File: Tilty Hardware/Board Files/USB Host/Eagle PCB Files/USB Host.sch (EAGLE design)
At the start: 14 parts, among them Q1 12MHz, U1 MAX3421E

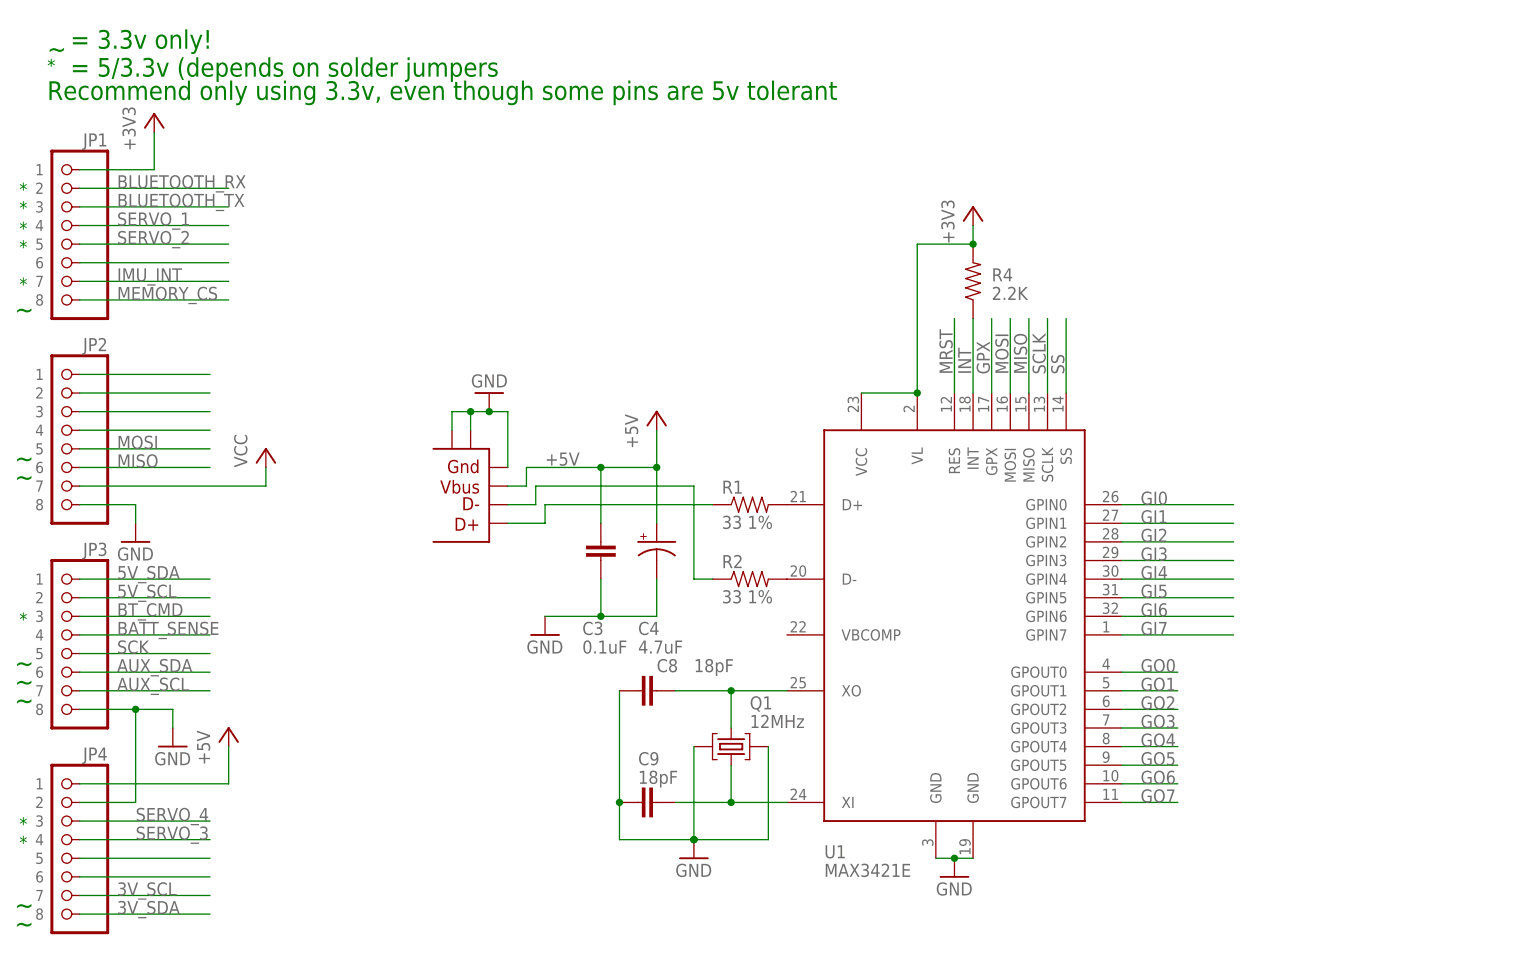
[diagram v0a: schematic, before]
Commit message: Added some datasheets, USB Host work
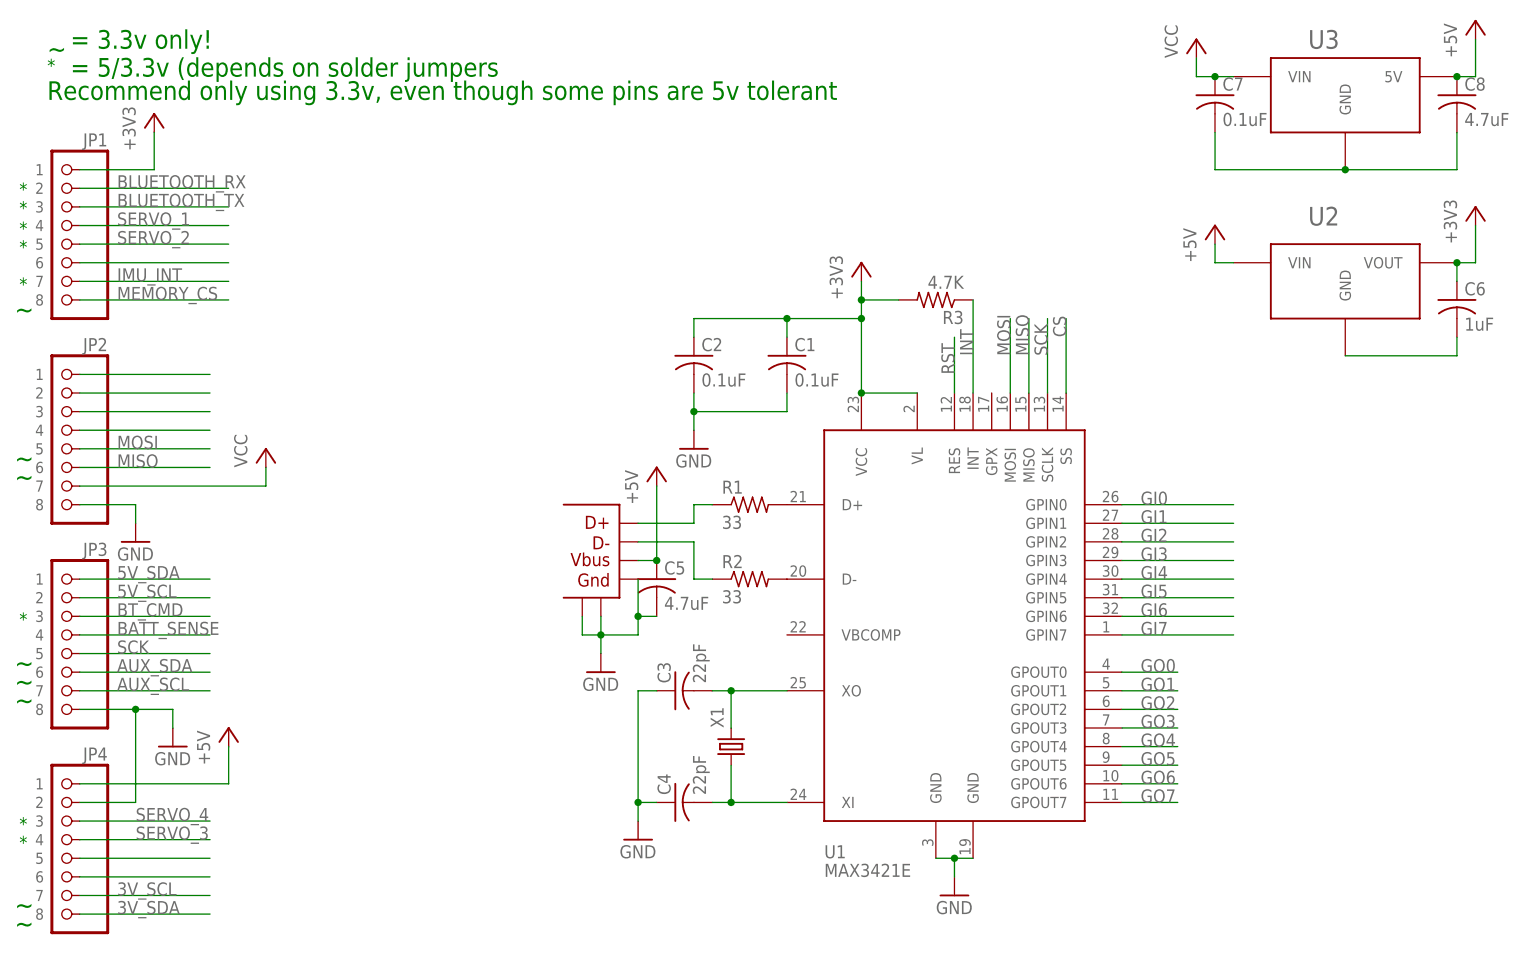
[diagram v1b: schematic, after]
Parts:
- removed C9: 18pF, CH_passive:CAP0603
- removed Q1: 12MHz, CH_passive:CRYSTAL_SH
- removed R4: 2.2K, CH_passive:RESISTOR0603
- added C1, C2, C7: 0.1uF, resistor:C-USC0603
- added C5: 4.7uF, resistor:C-USC0603
- added C6: 1uF, resistor:C-USC0603
- added R3: 4.7K, resistor:R-US_R0603
- added U2: AP7313SOT23R, My Parts:AP7313SOT23R
- added U3: LM2931, on-semiconductor:LM2931
- added X1: (no value), SparkFun-FreqCtrl:CRYSTALTXC-7A
- C3: value 0.1uF -> 22pF; device CH_passive:CAP0603 -> resistor:C-USC0603
- C4: value 4.7uF -> 22pF; device CH_passive:CAP_POL1206 -> resistor:C-USC0603
- C8: value 18pF -> 4.7uF; device CH_passive:CAP0603 -> resistor:C-USC0603
- R1, R2: value 33 1% -> 33; device CH_passive:RESISTOR0603 -> resistor:R-US_R0603
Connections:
- net MRST renamed RST
- net SS renamed CS
- removed net GPX: U1.GPX
- removed net N$40: C8.2, Q1.2, U1.XO
- removed net N$41: C9.2, Q1.1, U1.XI
- removed net SCLK: U1.SCLK
- new net N$11: C4.2, U1.XI, X1.1
- new net N$12: C3.2, U1.XO, X1.2
- new net N$15: C6.2, U2.GND
- new net N$16: C7.2, C8.2, U3.GND
- net +3V3: now also C1.1, C2.1, C6.1, R3.2, U2.VOUT; no longer R4.2
- net +5V: now also C5.1, C8.1, U2.VIN, U3.5V; no longer C3.1, C4.+
- net GND: now also C1.2, C2.2, C3.1, C4.1, C5.2; no longer C3.2, C4.-, C8.1, C9.1, Q1.3, Q1.4
- net INT: now also R3.1; no longer R4.1
- net SCK: now also U1.SCLK
- net VCC: now also C7.1, U3.VIN
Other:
- moved on the sheet: C3, C8

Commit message: Nearly finished USB Host
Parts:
- added D1: (no value), SparkFun-LED:LED-GREENLED-0805_NO_SILK
- added JP5, JP6: (no value), SparkFun-Connectors:M081X08
- added R4: (no value), resistor:R-US_R0603
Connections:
- removed net N$15: C6.2, U2.GND
- removed net N$16: C7.2, C8.2, U3.GND
- new net N$9: D1.A, R4.2
- net +5V: now also R4.1
- net GI0: now also JP5.1
- net GI1: now also JP5.2
- net GI2: now also JP5.3
- net GI3: now also JP5.4
- net GI4: now also JP5.5
- net GI5: now also JP5.6
- net GI6: now also JP5.7
- net GI7: now also JP5.8
- net GND: now also C6.2, C7.2, C8.2, D1.C, U2.GND, U3.GND
- net GO0: now also JP6.1
- net GO1: now also JP6.2
- net GO2: now also JP6.3
- net GO3: now also JP6.4
- net GO4: now also JP6.5
- net GO5: now also JP6.6
- net GO6: now also JP6.7
- net GO7: now also JP6.8
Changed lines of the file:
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@@
 <part name="P+5" library="supply1" deviceset="+5V" device=""/>
 <part name="P+6" library="supply1" deviceset="+5V" device=""/>
+<part name="JP5" library="SparkFun-Connectors" deviceset="M08" device="1X08"/>
+<part name="JP6" library="SparkFun-Connectors" deviceset="M08" device="1X08"/>
+<part name="GND6" library="supply1" deviceset="GND" device=""/>
+<part name="GND7" library="supply1" deviceset="GND" device=""/>
+<part name="D1" library="SparkFun-LED" deviceset="LED-GREEN" device="LED-0805_NO_SILK"/>
+<part name="R4" library="resistor" deviceset="R-US_" device="R0603"/>
+<part name="P+7" library="supply1" deviceset="+5V" device=""/>
+<part name="GND8" library="supply1" deviceset="GND" device=""/>
 </parts>
 <sheets>
@@
 <instance part="P+5" gate="1" x="160.02" y="96.52"/>
 <instance part="P+6" gate="1" x="195.58" y="124.46"/>
+<instance part="JP5" gate="G$1" x="167.64" y="50.8" rot="R180"/>
+<instance part="JP6" gate="G$1" x="160.02" y="27.94" rot="R180"/>
+<instance part="GND6" gate="1" x="185.42" y="73.66"/>
+<instance part="GND7" gate="1" x="182.88" y="99.06"/>
+<instance part="D1" gate="G$1" x="53.34" y="76.2" rot="R90"/>
+<instance part="R4" gate="G$1" x="45.72" y="76.2"/>
+<instance part="P+7" gate="1" x="38.1" y="81.28"/>
+<instance part="GND8" gate="1" x="60.96" y="71.12"/>
 </instances>
 <busses>
@@
 <pinref part="C3" gate="G$1" pin="1"/>
 <wire x1="81.28" y1="33.02" x2="83.82" y2="33.02" width="0.1524" layer="91"/>
+</segment>
+<segment>
+<pinref part="U2" gate="G$1" pin="GND"/>
+<pinref part="C6" gate="G$1" pin="2"/>
+<wire x1="177.8" y1="78.74" x2="185.42" y2="78.74" width="0.1524" layer="91"/>
+<wire x1="185.42" y1="78.74" x2="193.04" y2="78.74" width="0.1524" layer="91"/>
+<wire x1="193.04" y1="78.74" x2="193.04" y2="81.28" width="0.1524" layer="91"/>
+<pinref part="GND6" gate="1" pin="GND"/>
+<wire x1="185.42" y1="78.74" x2="185.42" y2="76.2" width="0.1524" layer="91"/>
+<junction x="185.42" y="78.74"/>
+</segment>
+<segment>
+<pinref part="U3" gate="G$1" pin="GND"/>
+<pinref part="C7" gate="G$1" pin="2"/>
+<wire x1="177.8" y1="104.14" x2="160.02" y2="104.14" width="0.1524" layer="91"/>
+<wire x1="160.02" y1="104.14" x2="160.02" y2="109.22" width="0.1524" layer="91"/>
+<pinref part="C8" gate="G$1" pin="2"/>
+<wire x1="177.8" y1="104.14" x2="182.88" y2="104.14" width="0.1524" layer="91"/>
+<wire x1="182.88" y1="104.14" x2="193.04" y2="104.14" width="0.1524" layer="91"/>
+<wire x1="193.04" y1="104.14" x2="193.04" y2="109.22" width="0.1524" layer="91"/>
+<junction x="177.8" y="104.14"/>
+<pinref part="GND7" gate="1" pin="GND"/>
+<wire x1="182.88" y1="101.6" x2="182.88" y2="104.14" width="0.1524" layer="91"/>
+<junction x="182.88" y="104.14"/>
+</segment>
+<segment>
+<pinref part="D1" gate="G$1" pin="C"/>
+<pinref part="GND8" gate="1" pin="GND"/>
+<wire x1="58.42" y1="76.2" x2="60.96" y2="76.2" width="0.1524" layer="91"/>
+<wire x1="60.96" y1="76.2" x2="60.96" y2="73.66" width="0.1524" layer="91"/>
 </segment>
 </net>
@@
 <wire x1="160.02" y1="91.44" x2="160.02" y2="93.98" width="0.1524" layer="91"/>
 </segment>
+<segment>
+<pinref part="R4" gate="G$1" pin="1"/>
+<pinref part="P+7" gate="1" pin="+5V"/>
+<wire x1="40.64" y1="76.2" x2="38.1" y2="76.2" width="0.1524" layer="91"/>
+<wire x1="38.1" y1="76.2" x2="38.1" y2="78.74" width="0.1524" layer="91"/>
+</segment>
 </net>
 <net name="VCC" class="0">
@@
 <label x="149.86" y="35.56" size="1.778" layer="95"/>
 <pinref part="U1" gate="G$1" pin="GPOUT0"/>
+<pinref part="JP6" gate="G$1" pin="1"/>
 </segment>
 </net>
@@
 <label x="149.86" y="33.02" size="1.778" layer="95"/>
 <pinref part="U1" gate="G$1" pin="GPOUT1"/>
+<pinref part="JP6" gate="G$1" pin="2"/>
 </segment>
 </net>
@@
 <label x="149.86" y="30.48" size="1.778" layer="95"/>
 <pinref part="U1" gate="G$1" pin="GPOUT2"/>
+<pinref part="JP6" gate="G$1" pin="3"/>
 </segment>
 </net>
@@
 <label x="149.86" y="27.94" size="1.778" layer="95"/>
 <pinref part="U1" gate="G$1" pin="GPOUT3"/>
+<pinref part="JP6" gate="G$1" pin="4"/>
 </segment>
 </net>
@@
 <label x="149.86" y="25.4" size="1.778" layer="95"/>
 <pinref part="U1" gate="G$1" pin="GPOUT4"/>
+<pinref part="JP6" gate="G$1" pin="5"/>
 </segment>
 </net>
@@
 <label x="149.86" y="22.86" size="1.778" layer="95"/>
 <pinref part="U1" gate="G$1" pin="GPOUT5"/>
+<pinref part="JP6" gate="G$1" pin="6"/>
 </segment>
 </net>
@@
 <label x="149.86" y="17.78" size="1.778" layer="95"/>
 <pinref part="U1" gate="G$1" pin="GPOUT7"/>
+<pinref part="JP6" gate="G$1" pin="8"/>
 </segment>
 </net>
@@
 <label x="149.86" y="20.32" size="1.778" layer="95"/>
 <pinref part="U1" gate="G$1" pin="GPOUT6"/>
+<pinref part="JP6" gate="G$1" pin="7"/>
 </segment>
 </net>
@@
 <label x="149.86" y="40.64" size="1.778" layer="95"/>
 <pinref part="U1" gate="G$1" pin="GPIN7"/>
+<pinref part="JP5" gate="G$1" pin="8"/>
 </segment>
 </net>
@@
 <label x="149.86" y="43.18" size="1.778" layer="95"/>
 <pinref part="U1" gate="G$1" pin="GPIN6"/>
+<pinref part="JP5" gate="G$1" pin="7"/>
 </segment>
 </net>
@@
 <label x="149.86" y="45.72" size="1.778" layer="95"/>
 <pinref part="U1" gate="G$1" pin="GPIN5"/>
+<pinref part="JP5" gate="G$1" pin="6"/>
 </segment>
 </net>
@@
 <label x="149.86" y="48.26" size="1.778" layer="95"/>
 <pinref part="U1" gate="G$1" pin="GPIN4"/>
+<pinref part="JP5" gate="G$1" pin="5"/>
 </segment>
 </net>
@@
 <label x="149.86" y="50.8" size="1.778" layer="95"/>
 <pinref part="U1" gate="G$1" pin="GPIN3"/>
+<pinref part="JP5" gate="G$1" pin="4"/>
 </segment>
 </net>
@@
 <label x="149.86" y="53.34" size="1.778" layer="95"/>
 <pinref part="U1" gate="G$1" pin="GPIN2"/>
+<pinref part="JP5" gate="G$1" pin="3"/>
 </segment>
 </net>
@@
 <label x="149.86" y="55.88" size="1.778" layer="95"/>
 <pinref part="U1" gate="G$1" pin="GPIN1"/>
+<pinref part="JP5" gate="G$1" pin="2"/>
 </segment>
 </net>
@@
 <label x="149.86" y="58.42" size="1.778" layer="95"/>
 <pinref part="U1" gate="G$1" pin="GPIN0"/>
+<pinref part="JP5" gate="G$1" pin="1"/>
 </segment>
 </net>
@@
 </segment>
 </net>
-<net name="N$15" class="0">
-<segment>
-<pinref part="U2" gate="G$1" pin="GND"/>
-<pinref part="C6" gate="G$1" pin="2"/>
-<wire x1="177.8" y1="78.74" x2="193.04" y2="78.74" width="0.1524" layer="91"/>
-<wire x1="193.04" y1="78.74" x2="193.04" y2="81.28" width="0.1524" layer="91"/>
-</segment>
-</net>
-<net name="N$16" class="0">
-<segment>
-<pinref part="U3" gate="G$1" pin="GND"/>
-<pinref part="C7" gate="G$1" pin="2"/>
-<wire x1="177.8" y1="104.14" x2="160.02" y2="104.14" width="0.1524" layer="91"/>
-<wire x1="160.02" y1="104.14" x2="160.02" y2="109.22" width="0.1524" layer="91"/>
-<pinref part="C8" gate="G$1" pin="2"/>
-<wire x1="177.8" y1="104.14" x2="193.04" y2="104.14" width="0.1524" layer="91"/>
-<wire x1="193.04" y1="104.14" x2="193.04" y2="109.22" width="0.1524" layer="91"/>
-<junction x="177.8" y="104.14"/>
-</segment>
-</net>
+<net name="N$9" class="0">
+<segment>
+<pinref part="D1" gate="G$1" pin="A"/>
+<pinref part="R4" gate="G$1" pin="2"/>
+</segment>
+</net>

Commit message: Restarting GPS + Micro SD add-on
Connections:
- removed net N$10: JP1.6
- net CS: now also JP1.6
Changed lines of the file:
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@@
-</segment>
-</net>
-<net name="N$10" class="0">
-<segment>
-<pinref part="JP1" gate="G$1" pin="6"/>
-<wire x1="5.08" y1="91.44" x2="25.4" y2="91.44" width="0.1524" layer="91"/>
 </segment>
 </net>
@@
 <label x="139.7" y="81.28" size="1.778" layer="95" rot="R90"/>
 </segment>
-</net>
+<segment>
+<pinref part="JP1" gate="G$1" pin="6"/>
+<wire x1="5.08" y1="91.44" x2="25.4" y2="91.44" width="0.1524" layer="91"/>
+</segment>
+</net>
